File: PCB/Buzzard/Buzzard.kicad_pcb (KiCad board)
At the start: 2 copper layers, 150.4 x 122.8 mm, 73 parts, among them J1 PJ-320A, J2 SDA, J3 SCL, J4 Haptic Buzz, J5 TrackPoint, J6 OLED, J7 LCD, J8 Battery, SW1 SW_DPST_x2, SW2 Reset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

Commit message: further work on pcb
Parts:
- J4: footprint Connector_PinHeader_1.00mm:PinHeader_1x05_P1.00mm_Vertical -> Buzzard:Pimoroni Haptic Buzz DRV2605L Driver
- JP11, JP12, JP2, JP3, JP5, JP6, JP7, JP8, SW1: moved to B.Cu
- moved JP15 424.8 mm to (-103.0, 14.1), turned to -90 degrees
- moved JP14 420.7 mm to (-100.3, 14.1), turned to -90 degrees
- moved J3 419.3 mm to (-147.1, -47.2)
- moved JP16 418.3 mm to (-105.7, 14.1), turned to -90 degrees
- moved JP13 408.4 mm to (-97.6, 14.1), turned to -90 degrees
- moved J6 403.7 mm to (-101.7, 17.1)
- moved J2 395.6 mm to (-138.7, -21.4)
- moved SW1 391.5 mm to (-98.5, -19.9)
- moved JP7 388.7 mm to (-103.0, 14.1), turned to 90 degrees
- moved JP5 385.8 mm to (-97.6, 14.1), turned to 90 degrees
- moved JP8 382.2 mm to (-105.7, 14.1), turned to 90 degrees
- moved JP6 381.3 mm to (-100.3, 14.1), turned to 90 degrees
- moved J8 377.0 mm to (-92.2, 16.0), turned to 90 degrees
- moved SW2 365.0 mm to (-138.3, 9.30), turned to 180 degrees
- moved J5 275.2 mm to (-48.2, 15.7), turned to 85 degrees
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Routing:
- net VCC: track 0.00 -> 72.6 mm, vias 0 -> 3
- net GND: track 0.00 -> 34.2 mm
- net SCL: track 0.00 -> 32.5 mm, vias 0 -> 1
- net TP_CLK: track 0.00 -> 27.3 mm
- net TP_DATA: track 0.00 -> 26.0 mm
- net SDA: track 0.00 -> 25.3 mm
- net Net-(C1-Pad2): track 0.00 -> 24.2 mm
- net BAT+: track 0.00 -> 20.1 mm, vias 0 -> 2
- net LCD_DI: track 0.00 -> 17.3 mm
- net COL4: track 0.00 -> 17.1 mm
- net LCD_CS: track 0.00 -> 17.1 mm
- net SERIAL: track 0.00 -> 17.1 mm
- net LCD_CLK: track 0.00 -> 17.1 mm
- net COL5: track 0.00 -> 17.1 mm
- net RESET: track 0.00 -> 16.5 mm, vias 0 -> 2
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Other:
- board size 150.4 x 122.8 mm -> 152.1 x 94.4 mm

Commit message: further work on the pcb
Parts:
- removed J2: SDA, Connector_PinHeader_2.54mm:PinHeader_1x01_P2.54mm_Vertical
- removed J3: SCL, Connector_PinHeader_2.54mm:PinHeader_1x01_P2.54mm_Vertical
- J7: value LCD -> Sharp Memory LCD Breakout; footprint Connector_PinHeader_1.00mm:PinHeader_1x08_P1.00mm_Vertical -> Buzzard:SharpMemoryLcdBreakout-Reversable
- JP10, SW2: moved to B.Cu
- JP11: value LCD CLK Jumper -> LCD CLK
- JP12: value LCD CS Jumper -> LCD CS; moved to F.Cu
- moved JP12 427.7 mm to (-108.4, 23.4), turned to 90 degrees
- moved JP11 422.0 mm to (-108.4, 23.4), turned to 90 degrees
- moved J7 413.7 mm to (-102.8, 18.0)
- moved JP10 403.7 mm to (-97.2, 23.4), turned to 90 degrees
- moved JP9 397.9 mm to (-97.2, 23.4), turned to 90 degrees
- moved SW2 27.9 mm to (-113.9, -4.20), turned to -90 degrees
- moved R2 20.6 mm to (-112.2, 17.3)
- moved R1 10.1 mm to (-115.5, 17.3)
- moved J6 1.04 mm to (-102.7, 16.8)
- moved JP13 0.92 mm to (-98.2, 13.4)
- moved JP14 0.92 mm to (-100.9, 13.4)
- moved JP5 0.92 mm to (-98.2, 13.4)
- moved JP6 0.92 mm to (-100.9, 13.4)
- moved JP15 0.92 mm to (-103.6, 13.4)
- moved JP16 0.92 mm to (-106.3, 13.4)
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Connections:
- J7 pad 1: VCC -> Net-(JP10-Pad2)
- J7 pad 2: unconnected-(J7-Pad2) -> GND
- J7 pad 3: GND -> LCD_DI
- J7 pad 4: Net-(J7-Pad4) -> VCC
- J7 pad 5: LCD_DI -> Net-(JP11-Pad2)
- JP10 pad 2: Net-(J7-Pad4) -> Net-(JP10-Pad2)
- JP11 pad 2: Net-(J7-Pad6) -> Net-(JP11-Pad2)
- JP12 pad 2: Net-(J7-Pad6) -> Net-(JP11-Pad2)
- JP9 pad 2: Net-(J7-Pad4) -> Net-(JP10-Pad2)
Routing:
- net LCD_DI: track 17.3 -> 67.8 mm, vias 0 -> 2
- net LCD_CS: track 17.1 -> 60.4 mm, vias 0 -> 3
- net LCD_CLK: track 17.1 -> 59.7 mm, vias 0 -> 2
- net VCC: track 72.6 -> 97.4 mm, vias 3 -> 5
- net SDA: track 25.3 -> 44.5 mm, vias 0 -> 2
- net SCL: track 32.5 -> 50.2 mm, vias 1 -> 3
- net RESET: track 16.5 -> 24.6 mm, vias 2 -> 3
- net Net-(JP10-Pad2): track 0.00 -> 6.14 mm
- net Net-(JP11-Pad2): track 0.00 -> 6.14 mm
- net Net-(J6-Pad4): track 0.00 -> 6.07 mm
- net Net-(J6-Pad3): track 0.00 -> 5.94 mm
- net Net-(J6-Pad2): track 0.00 -> 5.81 mm
- net Net-(J6-Pad1): track 0.00 -> 5.67 mm
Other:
- board text added: "LCD"

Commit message: further work
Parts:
- JP11: value LCD CLK -> LCD CLK Jumper
- JP12: value LCD CS -> LCD CS Jumper
- S1, S10, S5, S6, S9: footprint Buzzard:Kailh_socket_PG1350_optional_reversible.kicad_mod -> Buzzard:SW_PG1350_reversible
- SW2: footprint Buzzard:SMD-SW-4_5.1x5.1x2.5 -> Buzzard:SW_Tactile_SPST_Angled_PTS645Vx39-2LFS
- moved D10 246.5 mm to (187.7, -122.4)
- moved D12 246.5 mm to (178.9, -122.4)
- moved D15 246.5 mm to (161.8, -110.6)
- moved D1 246.5 mm to (196.9, -124.7)
- moved D11 246.5 mm to (236.2, -160.9)
- moved D13 246.5 mm to (166.0, -124.7)
- moved D14 246.5 mm to (154.7, -112.9)
- moved D16 246.5 mm to (154.8, -115.2)
- moved D17 246.5 mm to (186.0, -154.2)
- moved D18 246.5 mm to (188.1, -124.7)
- moved D2 246.5 mm to (179.3, -124.7)
- moved D3 246.5 mm to (170.6, -111.3)
- moved D4 246.5 mm to (178.9, -117.8)
- moved D5 246.5 mm to (187.7, -117.8)
- moved D6 246.5 mm to (178.9, -120.1)
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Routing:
- net SDA: track 44.5 -> 147.0 mm, vias 2 -> 7
- net SCL: track 50.2 -> 139.7 mm, vias 3 -> 10
- net TP_CLK: track 27.3 -> 107.6 mm, vias 0 -> 4
- net TP_DATA: track 26.0 -> 100.8 mm, vias 0 -> 4
- net VCC: track 97.4 -> 112.2 mm, vias 5 -> 6
- net RESET: track 24.6 -> 37.9 mm, vias 3 -> 4
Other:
- outline, holes or cut-outs redrawn

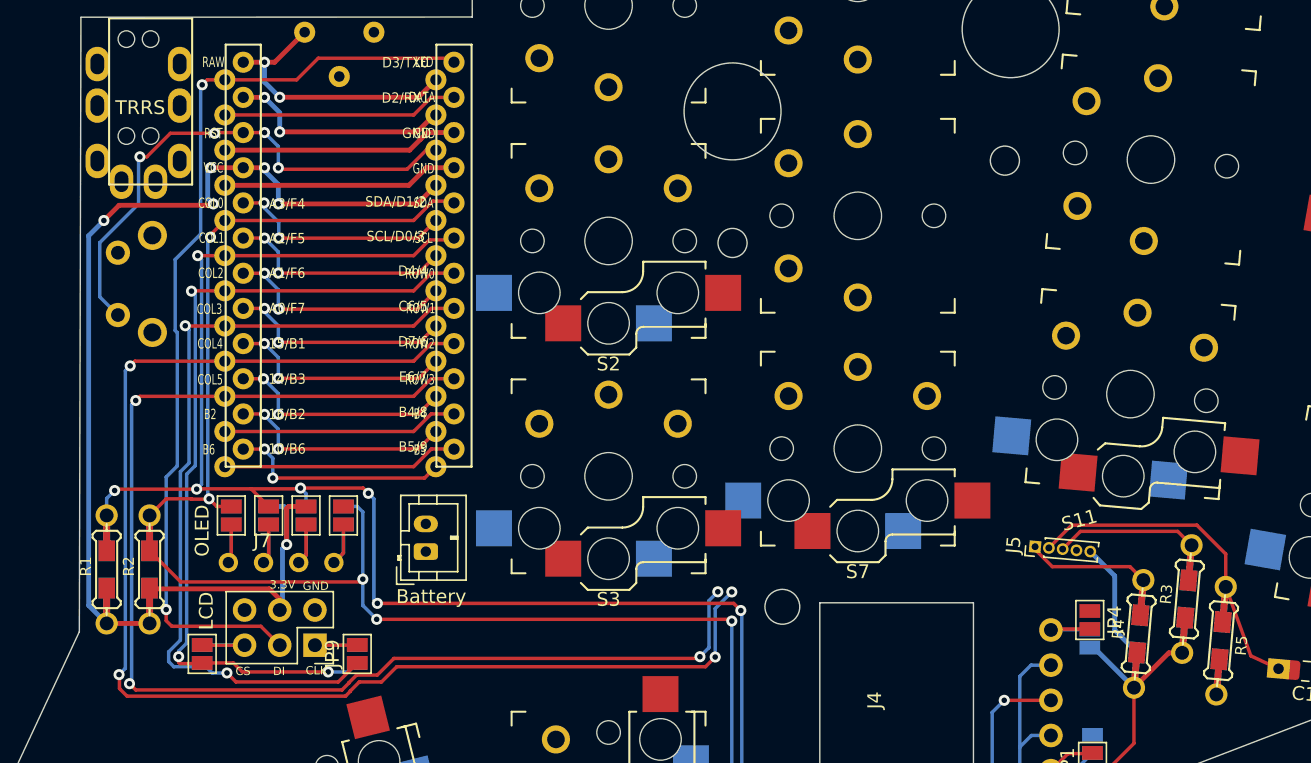
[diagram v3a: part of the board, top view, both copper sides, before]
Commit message: replaced trrs symbol and fixed connections
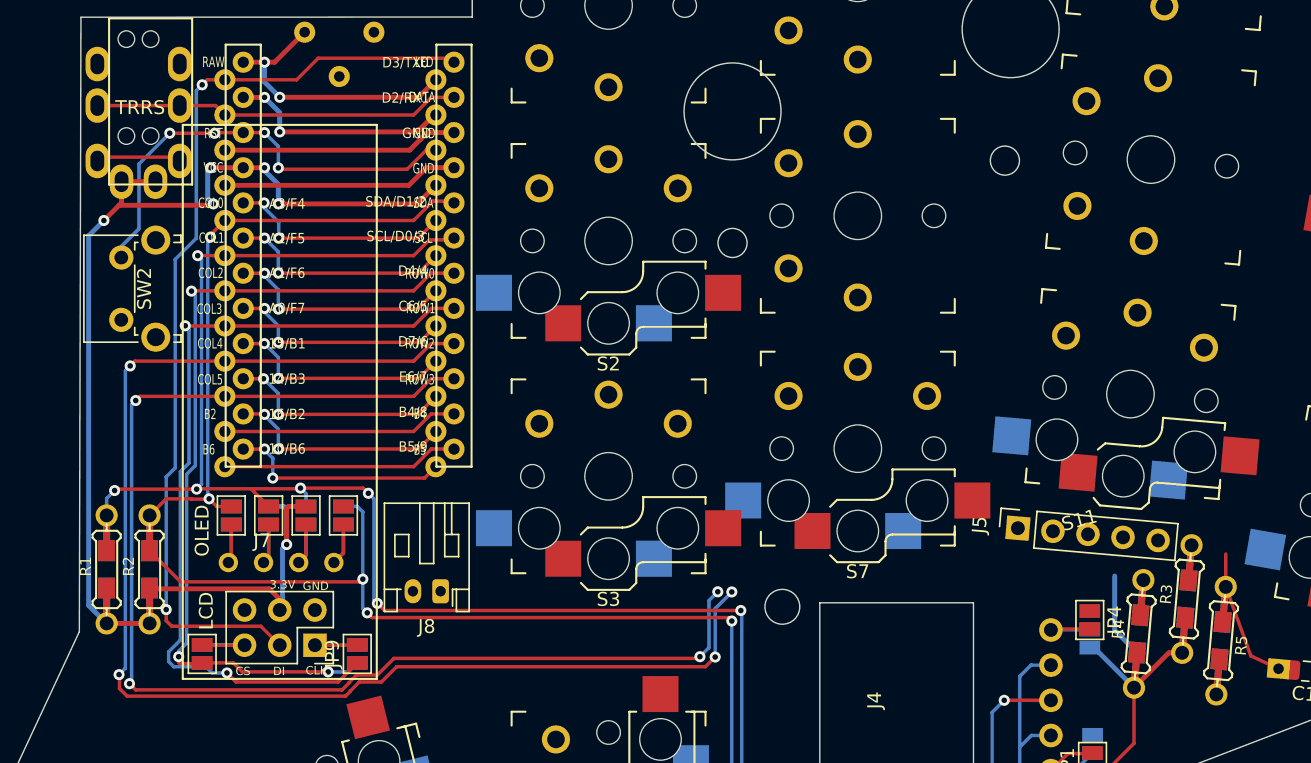
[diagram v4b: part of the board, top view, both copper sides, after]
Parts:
- J5: footprint Connector_PinHeader_1.00mm:PinHeader_1x05_P1.00mm_Vertical -> Connector_PinSocket_2.54mm:PinSocket_1x05_P2.54mm_Vertical
- J8: footprint Connector_JST:JST_PH_B2B-PH-K_1x02_P2.00mm_Vertical -> Connector_JST:JST_PH_S2B-PH-K_1x02_P2.00mm_Horizontal
- SW2: moved to F.Cu
- moved SW2 4.86 mm to (89.3, 74.8), turned to 90 degrees
- moved J8 3.06 mm to (112.4, 94.5), turned to 180 degrees
- moved J5 1.82 mm to (154.1, 89.9)
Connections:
- J1 pad 1: (no net) -> unconnected-(J1-Pad1)
- J1 pad 2: (no net) -> SERIAL
- J1 pad 3: (no net) -> GND
- J1 pad 4: (no net) -> VCC
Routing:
- net Net-(C1-Pad2): track 24.2 -> 9.88 mm
- net TP_CLK: track 107.6 -> 97.3 mm
- net SERIAL: track 17.1 -> 26.6 mm
- net TP_DATA: track 100.8 -> 91.9 mm
- net unconnected-(J1-Pad1): track 0.00 -> 6.18 mm
- net RESET: track 37.9 -> 32.3 mm
- net VCC: track 112.2 -> 113.9 mm

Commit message: replaced lcd footprint and fixed connections
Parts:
- removed J7: Sharp Memory LCD Breakout, Buzzard:SharpMemoryLcdBreakout-Reversable
- added J2: LCD, Buzzard:SharpMemoryLcdBreakout-Reversable, F.Cu at (100.9, 93.3)
- added JP17: LCD CLK Jumper, Jumper:SolderJumper-2_P1.3mm_Open_Pad1.0x1.5mm, B.Cu at (109.2, 98.1)
- added JP18: LCD CS Jumper, Jumper:SolderJumper-2_P1.3mm_Open_Pad1.0x1.5mm, F.Cu at (109.2, 98.1)
- added JP19: LCD CLK Jumper, Jumper:SolderJumper-2_P1.3mm_Open_Pad1.0x1.5mm, F.Cu at (95.7, 102.2)
- added JP20: LCD CS Jumper, Jumper:SolderJumper-2_P1.3mm_Open_Pad1.0x1.5mm, B.Cu at (95.7, 102.2)
- moved D8 278.4 mm to (95.1, 108.0)
- moved D4 244.4 mm to (85.4, 108.0), turned to -152 degrees
- moved D12 232.8 mm to (116.8, 102.0)
- moved R1 7.49 mm to (91.5, 86.1)
- moved R2 6.61 mm to (91.6, 99.5)
- moved JP10 6.20 mm to (101.0, 102.2)
- moved JP9 6.20 mm to (101.0, 102.2)
- moved JP11 4.53 mm to (98.3, 102.2)
- moved JP12 4.53 mm to (98.3, 102.2)
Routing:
- net ROW3: track 16.3 -> 58.3 mm, vias 2 -> 3
- net COL0: track 16.3 -> 53.6 mm, vias 2 -> 3
- net COL1: track 16.4 -> 49.6 mm, vias 2 -> 3
- net COL2: track 16.4 -> 48.2 mm, vias 2 -> 3
- net SCL: track 139.7 -> 155.8 mm, vias 10 -> 11
- net VCC: track 113.9 -> 127.2 mm, vias 6 -> 9
- net SDA: track 147.1 -> 154.9 mm, vias 7 -> 9
- net Net-(J2-Pad5): track 0.00 -> 6.91 mm
- net TP_DATA: track 91.9 -> 97.7 mm
- net Net-(J2-Pad1): track 0.00 -> 5.19 mm
- net TP_CLK: track 97.3 -> 101.8 mm
- net Net-(JP10-Pad2): track 6.14 -> 8.85 mm
- net LCD_CLK: track 59.9 -> 61.5 mm, vias 2 -> 3
- net Net-(JP11-Pad2): track 6.14 -> 6.91 mm

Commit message: placement of trackpoint circuit and thumb cluster
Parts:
- moved C1 6.55 mm to (168.3, 99.9), turned to 87.5 degrees
- moved R3 5.01 mm to (165.6, 100.0), turned to -92.5 degrees
- moved R5 2.36 mm to (170.8, 99.2), turned to 87.5 degrees
- moved R4 2.34 mm to (162.9, 99.9), turned to -92.5 degrees
- moved D4 1.00 mm to (84.4, 108.1), turned to -120 degrees
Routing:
- net COL1: track 49.6 -> 147.0 mm, vias 3 -> 8
- net COL2: track 48.2 -> 143.3 mm, vias 3 -> 7
- net COL0: track 53.6 -> 142.3 mm, vias 3 -> 7
- net TP_DATA: track 97.7 -> 135.2 mm, vias 4 -> 5
- net Net-(D12-Pad2): track 0.00 -> 37.0 mm
- net TP_CLK: track 101.8 -> 138.4 mm, vias 4 -> 5
- net ROW3: track 58.3 -> 91.6 mm
- net Net-(D8-Pad2): track 0.00 -> 30.7 mm
- net Net-(D4-Pad2): track 0.00 -> 30.1 mm
- net VCC: track 127.2 -> 137.6 mm, vias 9 -> 10
- net Net-(C1-Pad2): track 9.88 -> 19.4 mm

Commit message: further work
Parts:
- moved R2 28.8 mm to (120.3, 97.9), turned to 180 degrees
- moved JP17 3.94 mm to (106.2, 95.5)
- moved JP18 3.94 mm to (106.2, 95.5)
- moved D12 1.56 mm to (118.3, 101.9)
- moved D19 1.34 mm to (208.3, 101.1)
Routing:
- net VCC: track 137.6 -> 200.9 mm, vias 10 -> 13
- net Net-(J8-Pad1): track 0.00 -> 53.6 mm, vias 0 -> 3
- net COL0: track 142.3 -> 150.3 mm
- net Net-(D12-Pad2): track 37.0 -> 29.4 mm
- net TP_CLK: track 138.4 -> 143.9 mm
- net Net-(C1-Pad2): track 19.4 -> 23.7 mm, vias 0 -> 1
- net SCL: track 155.8 -> 159.7 mm
- net TP_DATA: track 135.2 -> 138.5 mm, vias 5 -> 6
- net COL1: track 147.0 -> 148.5 mm
- net LCD_DI: track 67.3 -> 66.1 mm
- net SDA: track 154.9 -> 153.8 mm, vias 9 -> 12
- net ROW3: track 91.6 -> 92.1 mm
- net Net-(J2-Pad1): track 5.19 -> 5.71 mm
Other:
- board size 152.1 x 94.4 mm -> 152.1 x 95.3 mm

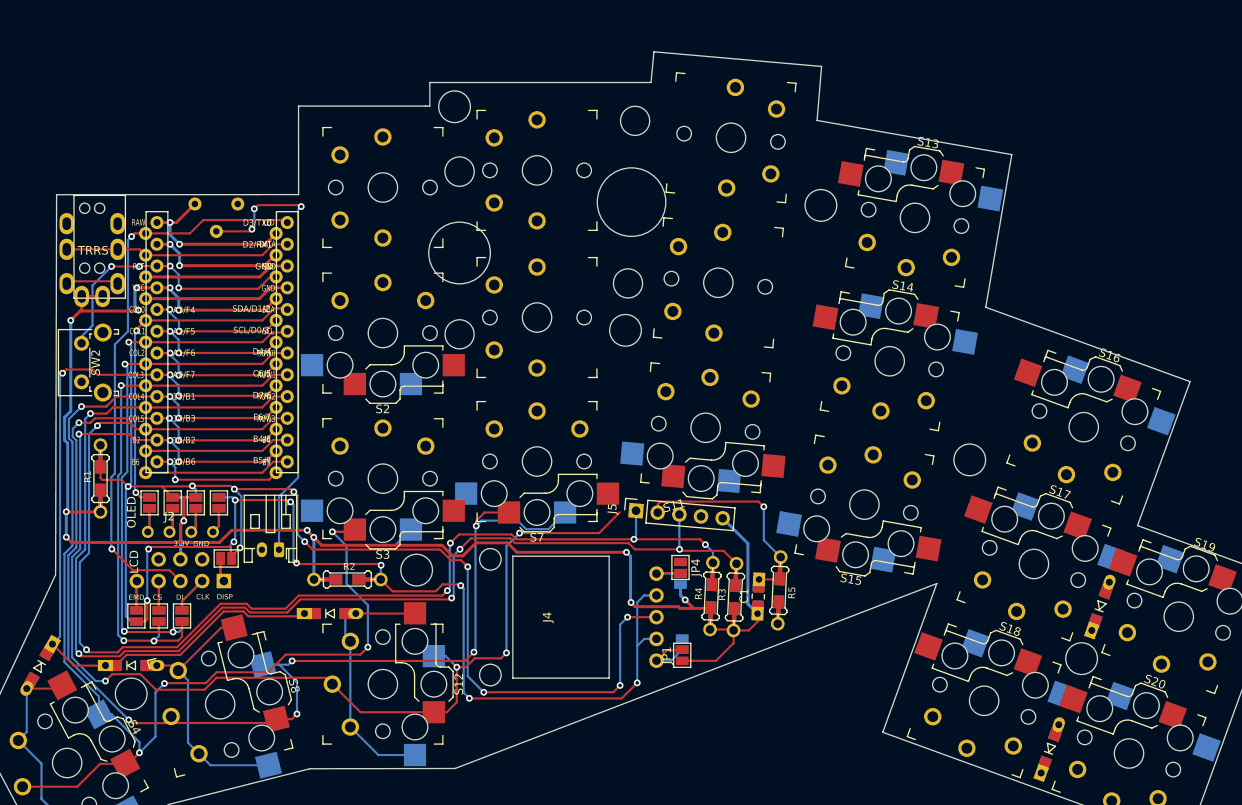
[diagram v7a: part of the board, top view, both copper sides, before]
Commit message: added mounting holes
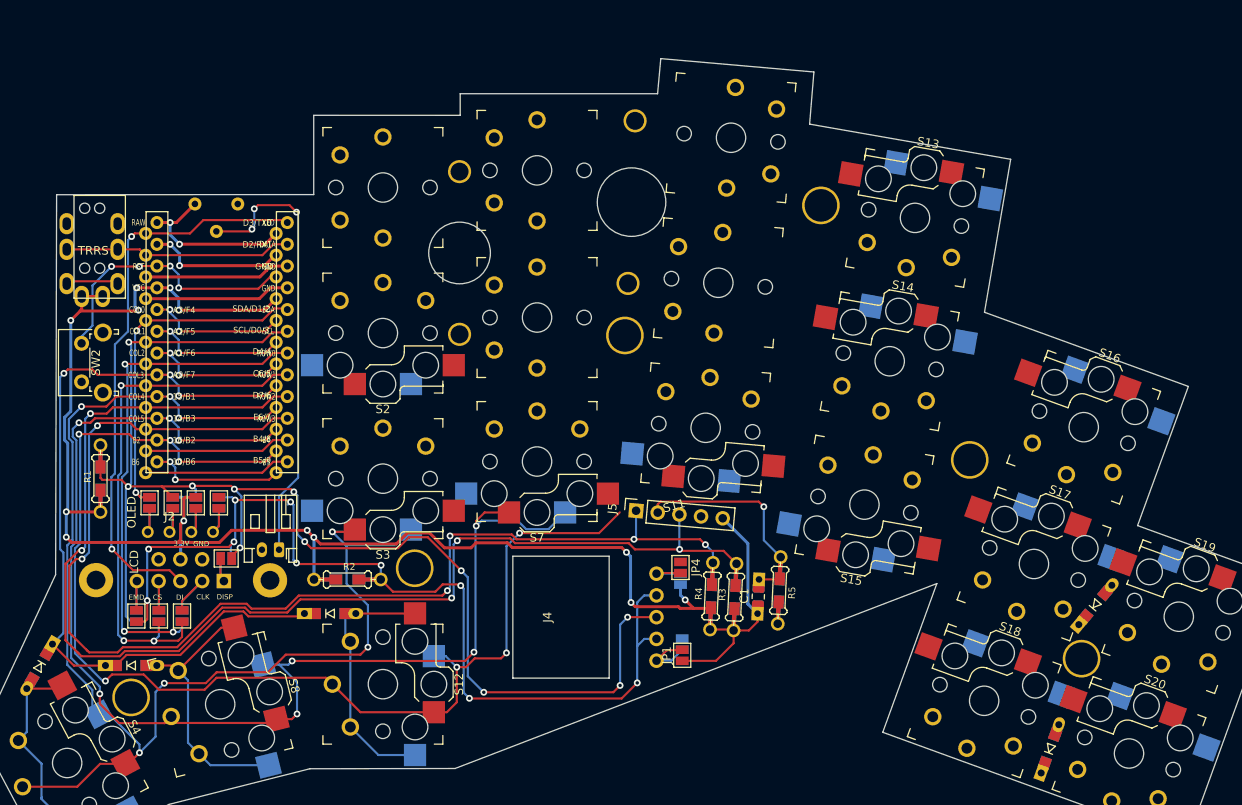
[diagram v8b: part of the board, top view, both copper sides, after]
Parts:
- added U10: Hole, Buzzard:HOLE_M2_TH, F.Cu at (153.1, 63.4)
- added U11: Hole, Buzzard:HOLE_M2_TH, F.Cu at (133.5, 69.3)
- added U12: Hole, Buzzard:HOLE_M2_TH, F.Cu at (133.5, 50.3)
- added U13: Hole, Buzzard:HOLE_M2_TH, F.Cu at (154.0, 44.4)
- added U2: Hole, Buzzard:M2_HOLE_PCB, F.Cu at (91.0, 98.0)
- added U3: Hole, Buzzard:M2_HOLE_PCB, F.Cu at (111.3, 98.0)
- added U4: Hole, Buzzard:HOLE_M2_TH, F.Cu at (206.1, 107.2)
- added U5: Hole, Buzzard:HOLE_M2_TH, F.Cu at (95.1, 111.7)
- added U6: Hole, Buzzard:HOLE_M2_TH, F.Cu at (128.2, 96.6)
- added U7: Hole, Buzzard:HOLE_M2_TH, F.Cu at (193.0, 84.0)
- added U8: Hole, Buzzard:HOLE_M2_TH, F.Cu at (175.7, 54.2)
- added U9: Hole, Buzzard:HOLE_M2_TH, F.Cu at (152.8, 69.4)
- moved D19 0.64 mm to (207.7, 100.9), turned to 50 degrees
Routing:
- net TP_CLK: track 143.9 -> 146.1 mm
- net TP_DATA: track 138.5 -> 140.6 mm
- net Net-(J8-Pad1): track 53.6 -> 52.6 mm
- net COL2: track 143.3 -> 142.5 mm
- net COL1: track 148.5 -> 149.1 mm
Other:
- board size 152.1 x 95.3 mm -> 152.1 x 94.5 mm
